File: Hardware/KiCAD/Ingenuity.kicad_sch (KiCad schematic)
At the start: 36 parts, among them J2 Conn_02x05_Odd_Even, J3 Conn_02x20_Odd_Even, J4 Conn_01x03, J5 Conn_01x03, J8 Conn_ST_STDC14, SW2 SW_Push, U2 STM32L412KBTx, U4 LSM6DSM

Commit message: changement kicad
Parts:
- added C7: 100n, Capacitor_SMD:C_0402_1005Metric, symbol Device:C_Small
- added J1: Conn_01x04, symbol Connector_Generic:Conn_01x04
- added R1: ?, Resistor_SMD:R_0402_1005Metric, symbol Device:R_Small
- added R9: 100k, Resistor_SMD:R_0402_1005Metric, symbol Device:R_Small
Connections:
- net GND: now also C7.2, J1.4 (Pin_4), R9.2
- net INT: now also U2.28 (PB5); no longer U2.21 (PA11)
- net TENSION_BATTERIE: now reaches U2.14 (PB0)
- net TENSION_BATTERIE: now also C7.1, R1.1, R9.1
- new net: J1.1 (Pin_1), R1.2
- no-connect marks 47 -> 48
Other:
- note added: "Mesure de tension"
- moved on the sheet: J4, J5

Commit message: pcb
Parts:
- removed C10, C11: 10u, Capacitor_SMD:C_0603_1608Metric, symbol Device:C_Polarized_Small
- removed D2, D4: LED, LED_SMD:LED_0603_1608Metric, symbol Device:LED
- removed R3: 375, Resistor_SMD:R_0402_1005Metric, symbol Device:R_Small
- removed R5: 250, Resistor_SMD:R_0402_1005Metric, symbol Device:R_Small
- removed U6: ~, symbol myLib:LDO_BU33TD3WG
- added C10, C8: 1u, Capacitor_SMD:C_0402_1005Metric, symbol Device:C_Small
- added C11: 100n, Capacitor_SMD:C_0402_1005Metric, symbol Device:C_Small
- added TP1, TP2, TP3, TP4, TP5, TP6: TestPoint, TestPoint:TestPoint_Pad_D1.5mm, symbol Connector:TestPoint
- added U3: BU33..., Package_TO_SOT_SMD:SOT-23-5, symbol Regulator_Linear:MIC5317-3.3xM5
- J1: footprint (none) -> Connector_JST:JST_XH_B4B-XH-A_1x04_P2.50mm_Vertical
- R1: value ? -> 27k
- R9: value 100k -> 10k
- U1: footprint mesmodules:Buck_17395xx36 -> myemp:Buck_ing
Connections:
- net +3.3V: now also C10.1, C11.2, U3.5 (VOUT)
- net +5V: now also C8.1, TP2.1, U3.1 (VIN), U3.3 (EN); no longer J5.2 (Pin_2)
- net +6V: now also J5.2 (Pin_2), TP1.1
- net GND: now also C10.2, C11.1, C8.2, U3.2 (GND)
- net SPI1_MISO: now also TP5.1
- net SPI1_MOSI: now also TP6.1
- net SPI1_SCK: now also TP4.1
- net SPI_CS: now also TP3.1
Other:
- note added: "6V comes from ESC"
- note added: "ESC Connector"
- note added: "Test points"

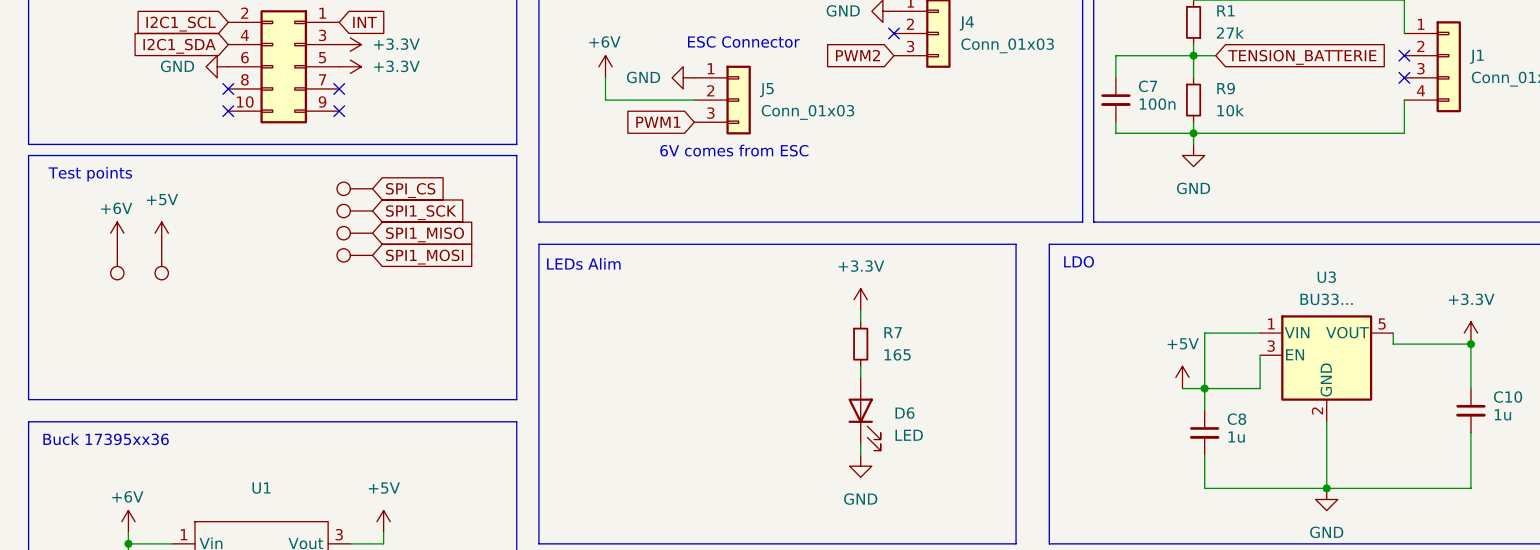
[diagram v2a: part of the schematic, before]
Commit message: maj BOM-MPN
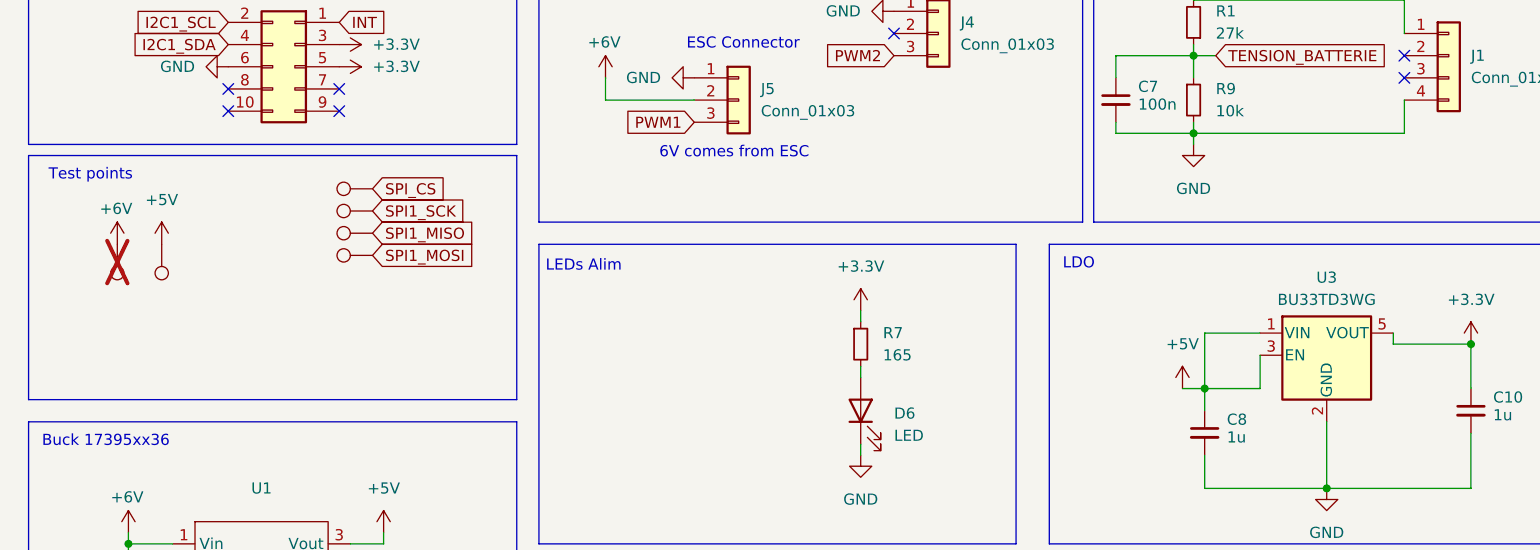
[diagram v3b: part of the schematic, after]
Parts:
- TP1: now not fitted
- U1: MPN (none) -> 173950536
- U3: value BU33... -> BU33TD3WG; MPN (none) -> BU33TD3WG-TR
- U4: MPN (none) -> LGA-14L
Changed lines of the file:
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@@
 			)
 		)
+		(property "MPN" " LGA-14L"
+			(at 228.6 120.65 0)
+			(effects
+				(font
+					(size 1.27 1.27)
+				)
+				(hide yes)
+			)
+		)
 		(pin "9"
 		)
@@
 		(in_bom yes)
 		(on_board yes)
-		(dnp no)
+		(dnp yes)
 		(fields_autoplaced yes)
 		(property "Reference" "TP1"
@@
 			)
 		)
+		(property "MPN" "173950536"
+			(at 43.18 158.75 0)
+			(effects
+				(font
+					(size 1.27 1.27)
+				)
+				(hide yes)
+			)
+		)
 		(pin "3"
 		)
@@
 			)
 		)
-		(property "Value" "BU33..."
+		(property "Value" "BU33TD3WG"
 			(at 165.1 130.81 0)
 			(effects
@@
 			(at 165.1 137.16 0)
 			(effects
+				(font
+					(size 1.27 1.27)
+				)
+				(hide yes)
+			)
+		)
+		(property "MPN" "BU33TD3WG-TR"
+			(at 165.1 137.16 0)
+			(effects

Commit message: update MPN BOMv3
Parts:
- U4: MPN LGA-14L -> LSM6DSMTR
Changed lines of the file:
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@@
 			)
 		)
-		(property "MPN" " LGA-14L"
+		(property "MPN" " LSM6DSMTR"
 			(at 228.6 120.65 0)
 			(effects

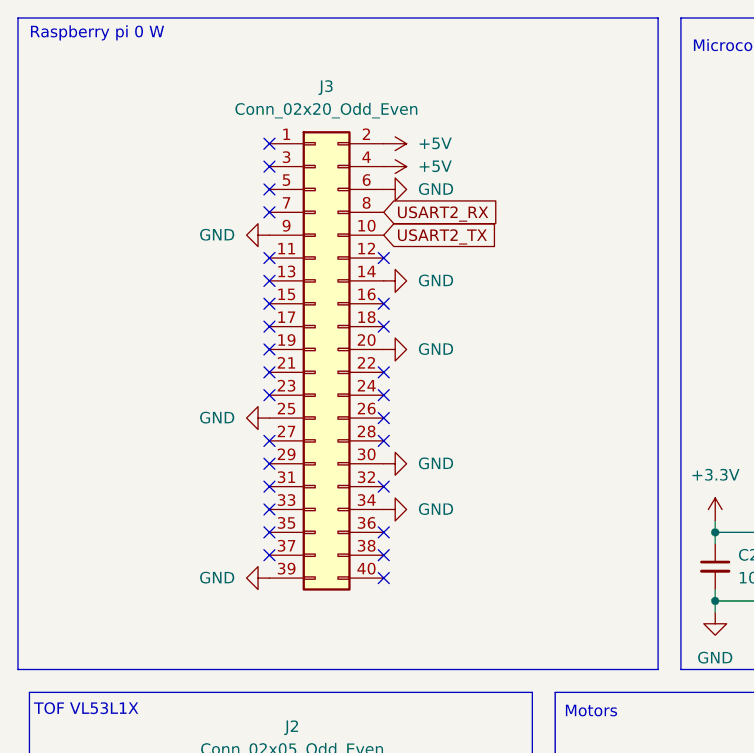
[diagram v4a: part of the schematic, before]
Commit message: update kicad reduction taille pcb
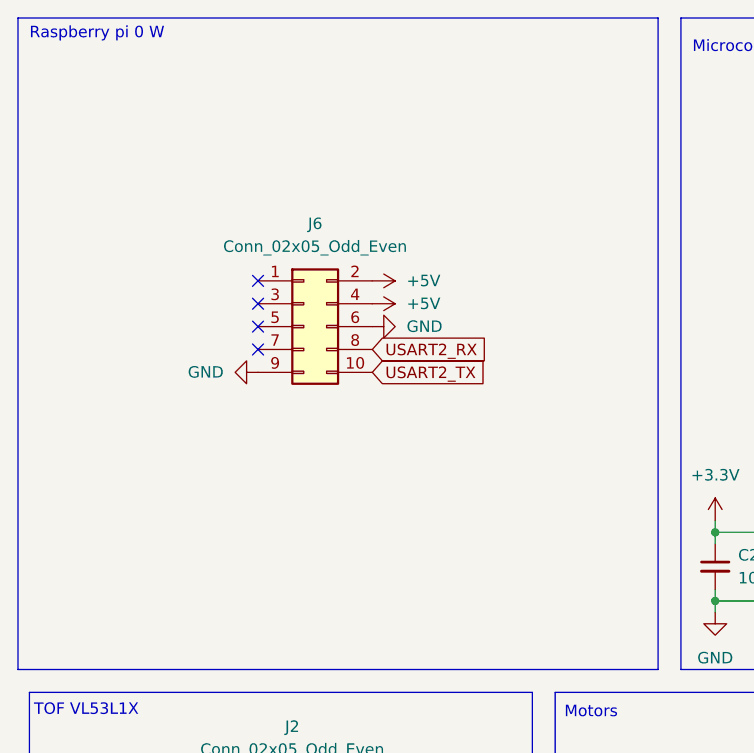
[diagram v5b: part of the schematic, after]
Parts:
- removed J3: Conn_02x20_Odd_Even, Connector_PinHeader_2.54mm:PinHeader_2x20_P2.54mm_Vertical, symbol Connector_Generic:Conn_02x20_Odd_Even
- added J6: Conn_02x05_Odd_Even, Connector_PinHeader_2.54mm:PinHeader_2x05_P2.54mm_Vertical, symbol Connector_Generic:Conn_02x05_Odd_Even
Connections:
- net +5V: now also J6.2 (Pin_2), J6.4 (Pin_4)
- net GND: now also J6.6 (Pin_6), J6.9 (Pin_9)
- net USART2_RX: now also J6.8 (Pin_8)
- net USART2_TX: now also J6.10 (Pin_10)
- no-connect marks 48 -> 24
